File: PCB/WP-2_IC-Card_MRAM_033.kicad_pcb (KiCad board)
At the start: 2 copper layers, 54 x 54 mm, 34 parts, among them J1 SMS-138-01-G-S, SW1 CUS-14B, U1 MRxA08xxYSxxx, U2 MIC5318-3.3YD5, U3 LVCH8T245, U4 LVCH8T245, U5 LVCH8T245, U6 LVCH8T245

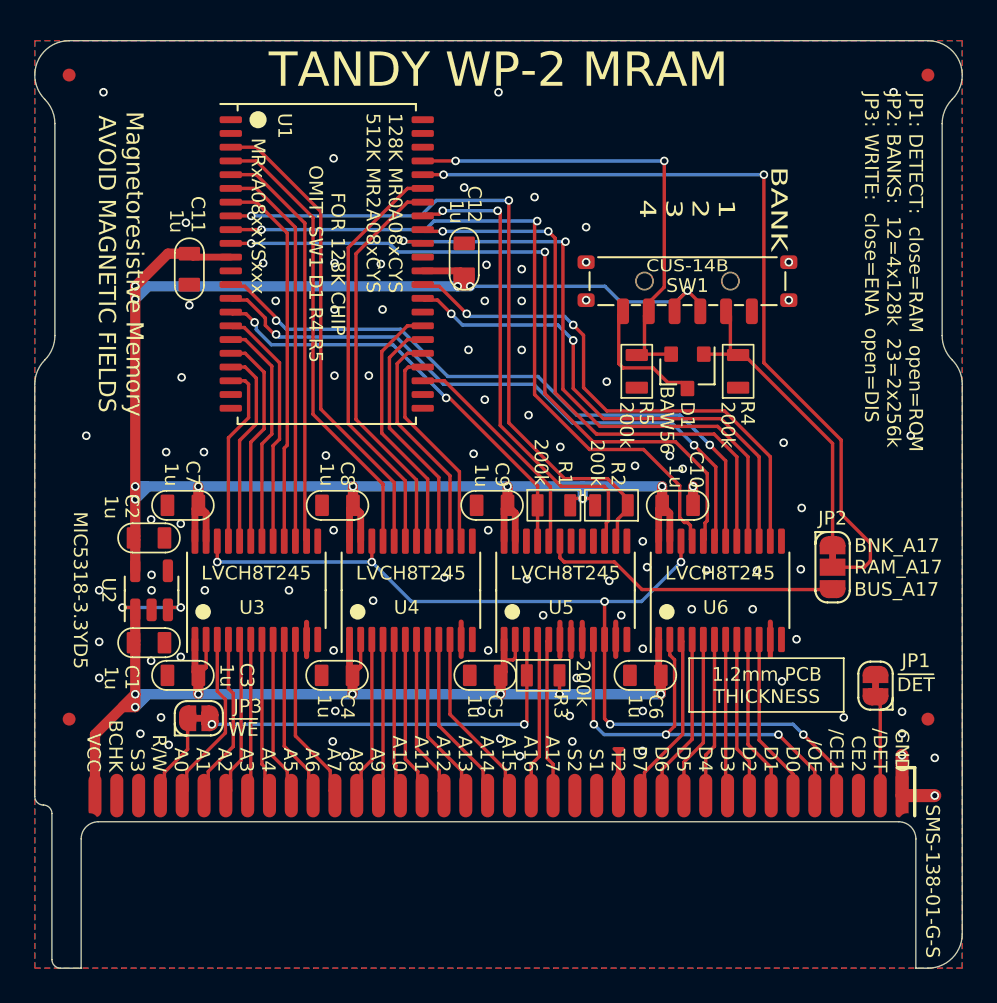
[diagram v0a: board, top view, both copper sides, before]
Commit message: MRAM: diodes, level shifters, ldo, docs
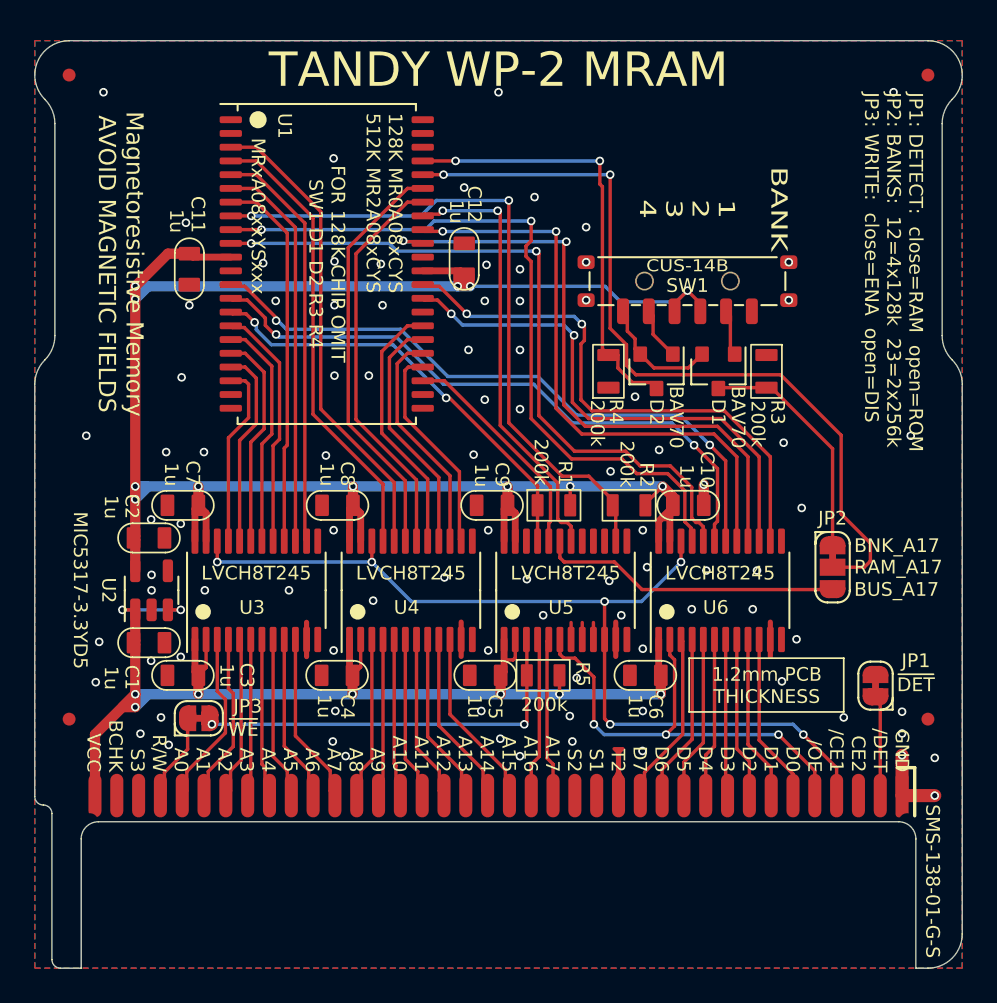
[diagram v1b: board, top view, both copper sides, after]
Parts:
- added D2: BAV70, 000_LOCAL:SOT-23, F.Cu at (145.2, 87.5)
- D1: value BAW56 -> BAV70
- U2: value MIC5318-3.3YD5 -> MIC5317-3.3YD5
- moved D1 1.80 mm to (148.8, 87.5)
- moved R3 1.65 mm to (151.6, 87.5), turned to -90 degrees
- moved R4 1.65 mm to (142.3, 87.5)
- moved R2 1.03 mm to (143.6, 95.3), turned to 0 degrees
- moved C10 0.62 mm to (147.0, 95.3)
- renumbered R4 to R3, R5 to R4, R3 to R5
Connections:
- D1 pad 1: /3A17bank -> /BANK_2
- D1 pad 2: /3A18 -> /BANK_4
- D1 pad 3: /BANK_4 -> /3A17bank
- SW1 pad 2: /3A17bank -> /BANK_2
- SW1 pad 5: /3A18 -> /BANK_3
- U5 pad 15: /~{3OE} -> unconnected-(U5-B7-Pad15)
- U5 pad 18: unconnected-(U5-B4-Pad18) -> /~{3OE}
- U5 pad 6: GND -> /~{OE}
- U5 pad 9: /~{OE} -> GND
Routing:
- net /3A17bank: track 18.7 -> 13.7 mm
- net /BANK_3: track 0.00 -> 3.07 mm
- net GND: track 22.0 -> 19.0 mm, vias 95 -> 91
- net /BANK_2: track 0.00 -> 2.70 mm
- net /3A18: track 28.3 -> 25.9 mm
- net /~{3OE}: track 28.0 -> 25.7 mm
- net /~{OE}: track 26.2 -> 27.4 mm
- net /~{3CE}: track 41.0 -> 39.9 mm
- net /3D5: track 31.1 -> 32.1 mm
- net /3D4: track 30.0 -> 30.8 mm
- net /3D7: track 34.0 -> 34.7 mm
- net /3D0: track 42.5 -> 43.2 mm
- net /BANK_4: track 7.75 -> 7.17 mm
- net /3D6: track 36.7 -> 37.2 mm
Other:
- board text added: "FOR 128K CHIP OMIT SW1 D1 D2 R3 R4"
- board text removed: "FOR 128K CHIP OMIT: SW1 D1 R4 R5"
